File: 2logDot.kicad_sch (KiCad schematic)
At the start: 7 parts, among them J1 RFID, J2 NEOPIXEL_RING, J3 Conn_01x14_Male, J4 Conn_01x13_Male, SW1 SOFT_RESET, U1 mini_esp32

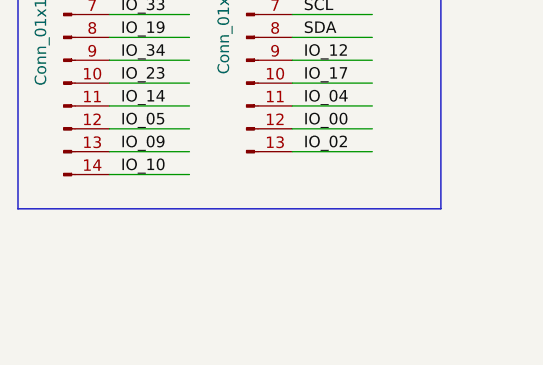
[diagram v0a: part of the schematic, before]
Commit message: added oled header
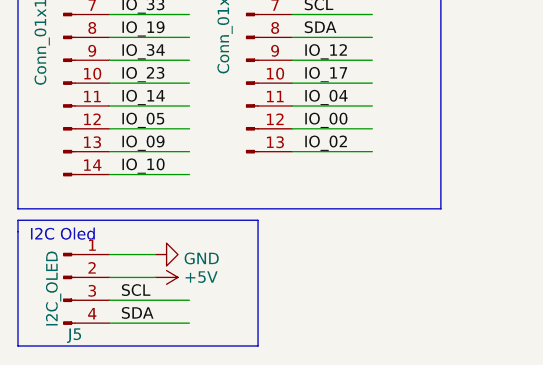
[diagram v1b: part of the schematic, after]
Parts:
- added J5: I2C_OLED, Connector_PinHeader_2.54mm:PinHeader_1x04_P2.54mm_Vertical, symbol Connector:Conn_01x04_Male
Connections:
- net +5V: now also J5.2 (Pin_2)
- net GND: now also J5.1 (Pin_1)
- net SCL: now also J5.3 (Pin_3)
- net SDA: now also J5.4 (Pin_4)
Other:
- note added: "I2C Oled"
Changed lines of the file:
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@@
+    (stroke (width 0) (type default) (color 0 0 0 0))
+  )
+  (polyline (pts (xy 53.34 106.68) (xy 26.67 106.68))
     (stroke (width 0) (type default) (color 0 0 0 0))
   )
@@
     (stroke (width 0) (type default) (color 0 0 0 0))
   )
+  (polyline (pts (xy 26.67 93.98) (xy 26.67 106.68))
+    (stroke (width 0) (type default) (color 0 0 0 0))
+  )
   (wire (pts (xy 111.76 36.83) (xy 120.65 36.83))
     (stroke (width 0) (type default) (color 0 0 0 0))
@@
     (stroke (width 0) (type default) (color 0 0 0 0))
   )
+  (wire (pts (xy 36.83 99.06) (xy 41.91 99.06))
+    (stroke (width 0) (type default) (color 0 0 0 0))
+  )
   (polyline (pts (xy 58.42 44.45) (xy 26.67 44.45))
     (stroke (width 0) (type default) (color 0 0 0 0))
@@
     (stroke (width 0) (type default) (color 0 0 0 0))
   )
+  (wire (pts (xy 36.83 96.52) (xy 41.91 96.52))
+    (stroke (width 0) (type default) (color 0 0 0 0))
+  )
   (wire (pts (xy 149.86 27.94) (xy 149.86 29.21))
     (stroke (width 0) (type default) (color 0 0 0 0))
@@
     (stroke (width 0) (type default) (color 0 0 0 0))
   )
+  (polyline (pts (xy 26.67 92.71) (xy 53.34 92.71))
+    (stroke (width 0) (type default) (color 0 0 0 0))
+  )
   (polyline (pts (xy 73.66 91.44) (xy 26.67 91.44))
     (stroke (width 0) (type default) (color 0 0 0 0))
@@
     (stroke (width 0) (type default) (color 0 0 0 0))
   )
+  (wire (pts (xy 36.83 104.14) (xy 45.72 104.14))
+    (stroke (width 0) (type default) (color 0 0 0 0))
+  )
   (wire (pts (xy 57.15 62.23) (xy 66.04 62.23))
     (stroke (width 0) (type default) (color 0 0 0 0))
@@
     (stroke (width 0) (type default) (color 0 0 0 0))
   )
+  (wire (pts (xy 36.83 101.6) (xy 45.72 101.6))
+    (stroke (width 0) (type default) (color 0 0 0 0))
+  )
   (wire (pts (xy 36.83 62.23) (xy 45.72 62.23))
     (stroke (width 0) (type default) (color 0 0 0 0))
@@
     (stroke (width 0) (type default) (color 0 0 0 0))
   )
+  (polyline (pts (xy 26.67 92.71) (xy 26.67 93.98))
+    (stroke (width 0) (type default) (color 0 0 0 0))
+  )
   (polyline (pts (xy 26.67 45.72) (xy 73.66 45.72))
     (stroke (width 0) (type default) (color 0 0 0 0))
@@
     (stroke (width 0) (type default) (color 0 0 0 0))
   )
+  (polyline (pts (xy 53.34 92.71) (xy 53.34 106.68))
+    (stroke (width 0) (type default) (color 0 0 0 0))
+  )
   (wire (pts (xy 95.25 46.99) (xy 95.25 44.45))
     (stroke (width 0) (type default) (color 0 0 0 0))
@@
     (stroke (width 0) (type default) (color 0 0 0 0))
   )
+  (text "I2C Oled" (at 27.94 95.25 0)
+    (effects (font (size 1.27 1.27)) (justify left bottom))
+  )
   (text "ESP32 Mini (Wemos D1 Format)" (at 92.71 24.13 0)
     (effects (font (size 1.27 1.27)) (justify left bottom))
@@
     (effects (font (size 1.27 1.27)) (justify left bottom))
   )
+  (label "SDA" (at 38.1 104.14 0)
+    (effects (font (size 1.27 1.27)) (justify left bottom))
+  )
   (label "IO_09" (at 113.03 39.37 0)
     (effects (font (size 1.27 1.27)) (justify left bottom))
@@
   )
   (label "IO_05" (at 38.1 82.55 0)
+    (effects (font (size 1.27 1.27)) (justify left bottom))
+  )
+  (label "SCL" (at 38.1 101.6 0)
     (effects (font (size 1.27 1.27)) (justify left bottom))
   )
@@
     )
     (pin "1")
+  )
+  (symbol (lib_id "Connector:Conn_01x04_Male") (at 31.75 99.06 0) (unit 1)
+    (in_bom yes) (on_board yes)
+    (property "Reference" "J5" (id 0) (at 33.02 105.41 0))
+    (property "Value" "I2C_OLED" (id 1) (at 30.48 100.33 90))
+    (property "Footprint" "Connector_PinHeader_2.54mm:PinHeader_1x04_P2.54mm_Vertical" (id 2) (at 31.75 99.06 0)
+      (effects (font (size 1.27 1.27)) hide)
+    )
+    (property "Datasheet" "~" (id 3) (at 31.75 99.06 0)
+      (effects (font (size 1.27 1.27)) hide)
+    )
+    (pin "1")
+    (pin "2")
+    (pin "3")
+    (pin "4")
   )
   (symbol (lib_id "power:+5V") (at 81.28 33.02 270) (unit 1)
@@
     (pin "1")
   )
+  (symbol (lib_id "power:GND") (at 41.91 96.52 90) (unit 1)
+    (in_bom yes) (on_board yes) (fields_autoplaced)
+    (property "Reference" "#PWR0114" (id 0) (at 48.26 96.52 0)
+      (effects (font (size 1.27 1.27)) hide)
+    )
+    (property "Value" "GND" (id 1) (at 45.085 96.999 90)
+      (effects (font (size 1.27 1.27)) (justify right))
+    )
+    (property "Footprint" "" (id 2) (at 41.91 96.52 0)
+      (effects (font (size 1.27 1.27)) hide)
+    )
+    (property "Datasheet" "" (id 3) (at 41.91 96.52 0)
+      (effects (font (size 1.27 1.27)) hide)
+    )
+    (pin "1")
+  )
   (symbol (lib_id "power:GND") (at 49.53 34.29 90) (unit 1)
     (in_bom yes) (on_board yes) (fields_autoplaced)
@@
     (pin "2")
   )
+  (symbol (lib_id "power:+5V") (at 41.91 99.06 270) (unit 1)
+    (in_bom yes) (on_board yes)
+    (property "Reference" "#PWR0115" (id 0) (at 38.1 99.06 0)
+      (effects (font (size 1.27 1.27)) hide)
+    )
+    (property "Value" "+5V" (id 1) (at 46.99 99.06 90))
+    (property "Footprint" "" (id 2) (at 41.91 99.06 0)
+      (effects (font (size 1.27 1.27)) hide)
+    )
+    (property "Datasheet" "" (id 3) (at 41.91 99.06 0)
+      (effects (font (size 1.27 1.27)) hide)
+    )
+    (pin "1")
+  )
   (sheet_instances
     (path "/" (page "1"))
@@
       (reference "#PWR0113") (unit 1) (value "+3V3") (footprint "")
     )
+    (path "/834390ba-6135-47e2-b0bf-fd6c03b8dba3"
+      (reference "#PWR0114") (unit 1) (value "GND") (footprint "")
+    )
+    (path "/e98fb1e9-dcb3-4943-b5e9-ac5075fe1d4f"
+      (reference "#PWR0115") (unit 1) (value "+5V") (footprint "")
+    )
     (path "/05c22087-f0be-4bf7-8f3e-adf8b92618f3"
       (reference "C1") (unit 1) (value "10u+") (footprint "Capacitor_SMD:CP_Elec_5x3")
@@
       (reference "J4") (unit 1) (value "Conn_01x13_Male") (footprint "Connector_PinSocket_2.54mm:PinSocket_1x13_P2.54mm_Vertical")
     )
+    (path "/34937f78-0cd7-450b-8935-ad6822032278"
+      (reference "J5") (unit 1) (value "I2C_OLED") (footprint "Connector_PinHeader_2.54mm:PinHeader_1x04_P2.54mm_Vertical")
+    )
     (path "/e322e877-fa4b-40a1-b9eb-04bd2db5ed6c"
